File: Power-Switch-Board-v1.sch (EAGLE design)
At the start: 7 parts, among them U3 CPH3356-TL-W

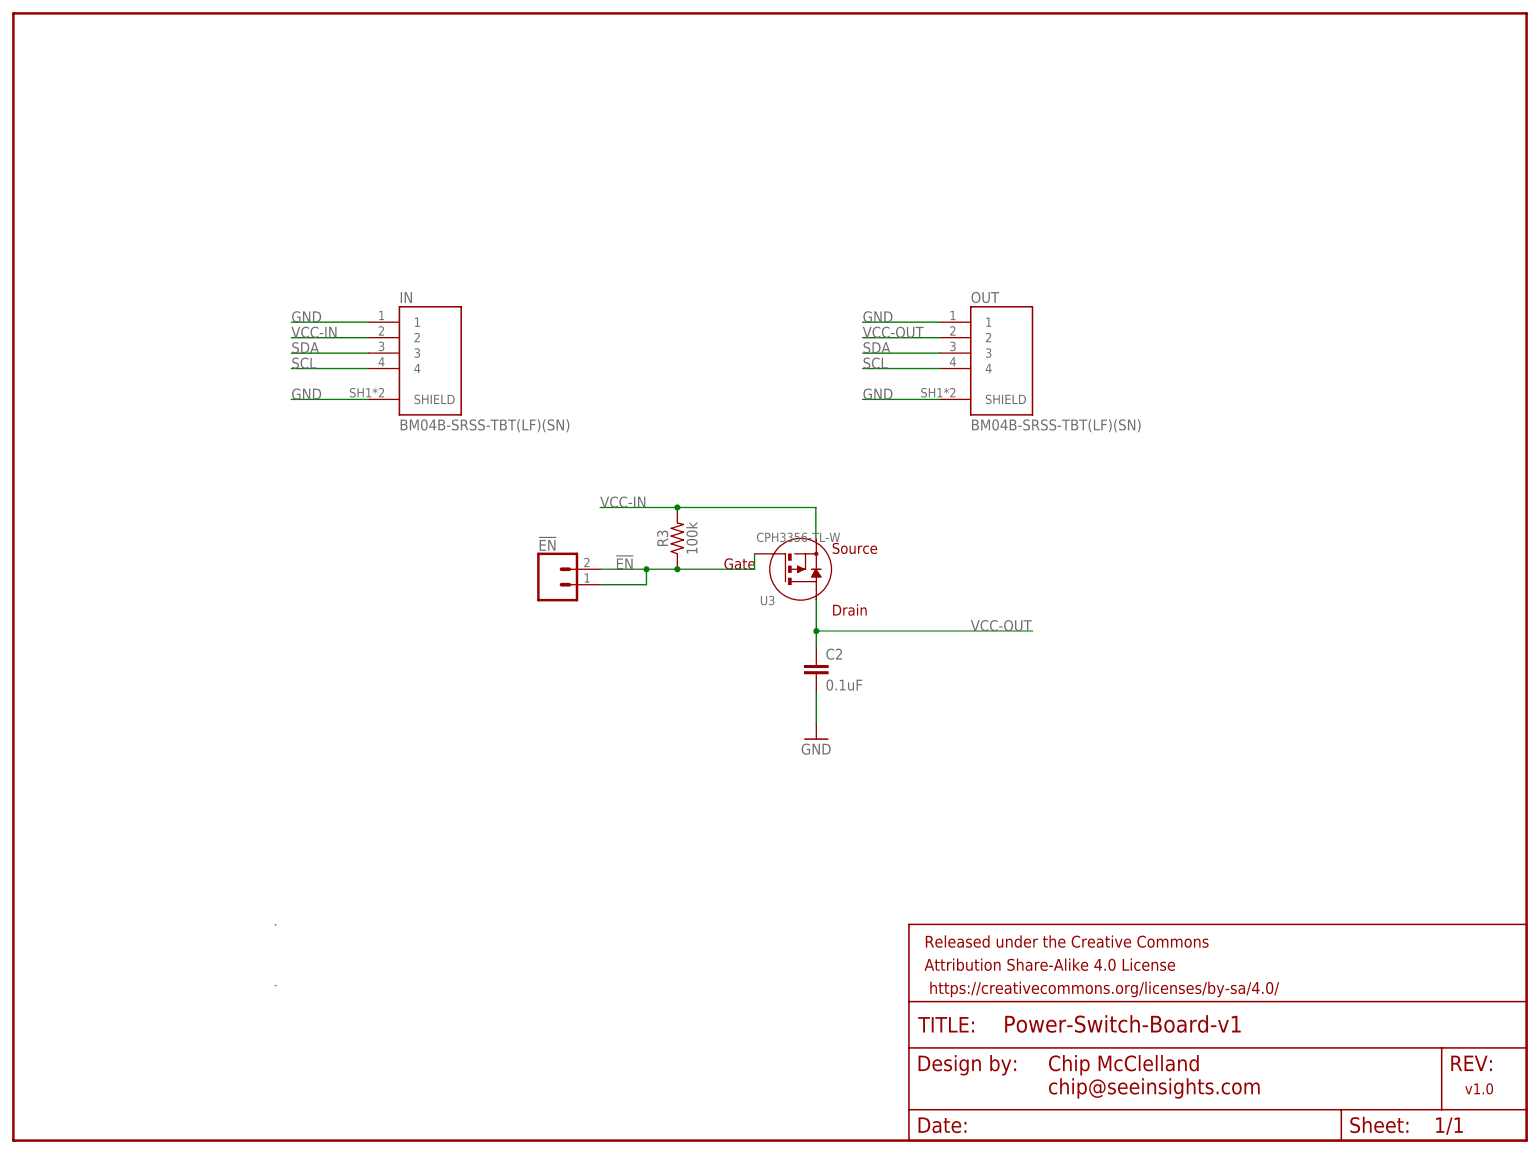
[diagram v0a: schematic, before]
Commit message: Updated for 0.1" headers
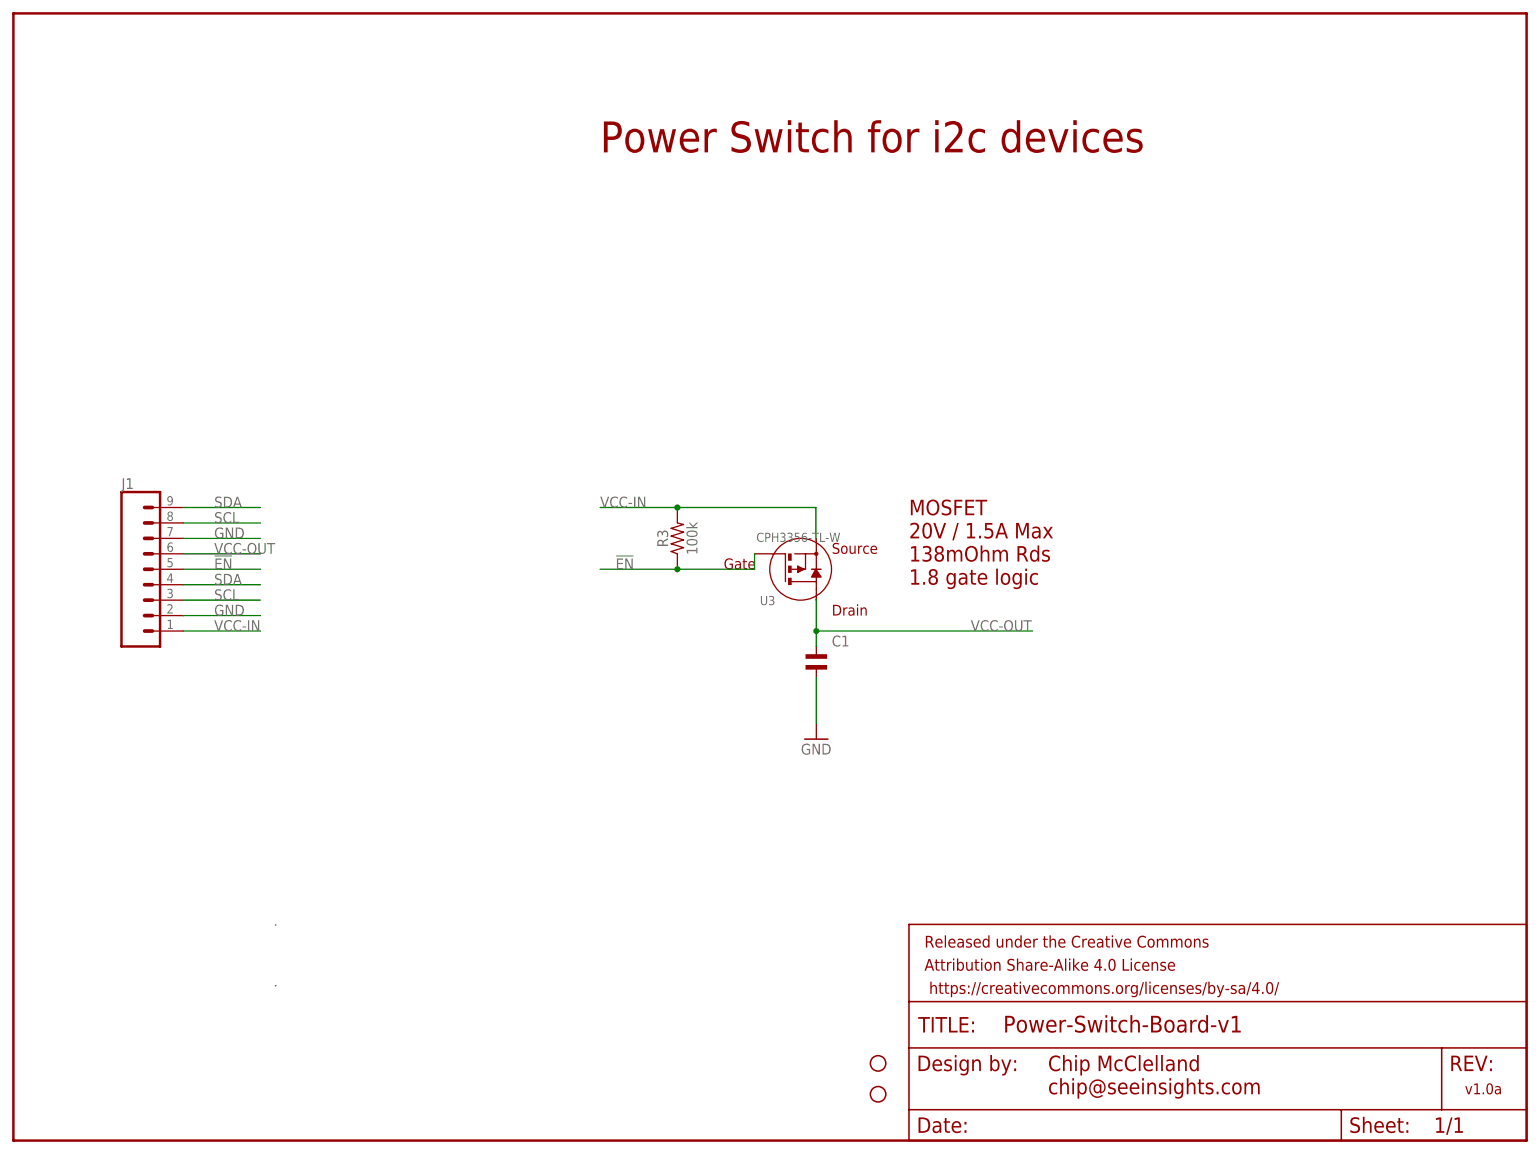
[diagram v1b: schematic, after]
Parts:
- removed !EN: (no value), SparkFun-Connectors:CONN_02
- removed C2: 0.1uF, Custom Components:CAP-MF-0.1UF-0805
- removed IN, OUT: BM04B-SRSS-TBT(LF)(SN), Custom Components:BM04B-SRSS-TBT(LF)(SN)
- added C1: (no value), Custom Components:CAP-MF-0.1UF-
- added H1, H2: STAND-OFF-M2.5, Custom Components:STAND-OFF-M2.5
- added J1: (no value), SparkFun-Connectors:CONN_09
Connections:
- net !EN: now also J1.5; no longer !EN.1, !EN.2
- net GND: now also C1.P$2, J1.2, J1.7; no longer C2.2, IN.1, IN.SHIELD, OUT.1, OUT.SHIELD
- net SCL: now also J1.3, J1.8; no longer IN.4, OUT.4
- net SDA: now also J1.4, J1.9; no longer IN.3, OUT.3
- net VCC-IN: now also J1.1; no longer IN.2
- net VCC-OUT: now also C1.P$1, J1.6; no longer C2.1, OUT.2
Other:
- note added: "MOSFET 20V / 1.5A Max 138mOhm Rds 1.8 gate logic"
- note added: "Power Switch for i2c devices"
- note added: "v1.0a"
- note removed: "v1.0"
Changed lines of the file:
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@@
 <part name="FRAME1" library="SparkFun-Aesthetics" library_urn="urn:adsk.eagle:library:507" deviceset="FRAME-LETTER" device="" package3d_urn="urn:adsk.eagle:package:37121/1"/>
 <part name="GND4" library="SparkFun-PowerSymbols" library_urn="urn:adsk.eagle:library:530" deviceset="GND" device=""/>
-<part name="C2" library="Custom Components" deviceset="CAP-MF-0.1UF-" device="0805" value="0.1uF"/>
 <part name="U3" library="Custom Components" deviceset="CPH3356-TL-W" device=""/>
 <part name="R3" library="Custom Components" deviceset="RESISTOR-MF-100K-" device="0805" package3d_urn="urn:adsk.eagle:package:39651/1" value="100k"/>
-<part name="IN" library="Custom Components" deviceset="BM04B-SRSS-TBT(LF)(SN)" device=""/>
-<part name="OUT" library="Custom Components" deviceset="BM04B-SRSS-TBT(LF)(SN)" device=""/>
-<part name="!EN" library="SparkFun-Connectors" library_urn="urn:adsk.eagle:library:513" deviceset="CONN_02" device="" package3d_urn="urn:adsk.eagle:package:38039/1"/>
+<part name="J1" library="SparkFun-Connectors" library_urn="urn:adsk.eagle:library:513" deviceset="CONN_09" device="" package3d_urn="urn:adsk.eagle:package:38153/1"/>
+<part name="H1" library="Custom Components" deviceset="STAND-OFF-M2.5" device="" package3d_urn="urn:adsk.eagle:package:38630/1"/>
+<part name="H2" library="Custom Components" deviceset="STAND-OFF-M2.5" device="" package3d_urn="urn:adsk.eagle:package:38630/1"/>
+<part name="C1" library="Custom Components" deviceset="CAP-MF-0.1UF-" device=""/>
 </parts>
 <sheets>
 <sheet>
 <plain>
-<text x="238.76" y="7.62" size="1.778" layer="94">v1.0</text>
+<text x="238.76" y="7.62" size="1.778" layer="94">v1.0a</text>
 <text x="170.18" y="7.62" size="2.54" layer="94">Chip McClelland
 chip@seeinsights.com</text>
+<text x="96.52" y="162.56" size="5.08" layer="94">Power Switch for i2c devices</text>
+<text x="147.32" y="91.44" size="2.54" layer="94">MOSFET
+20V / 1.5A Max
+138mOhm Rds
+1.8 gate logic</text>
 </plain>
 <instances>
@@
 <attribute name="VALUE" x="129.54" y="63.5" size="1.778" layer="96"/>
 </instance>
-<instance part="C2" gate="G$1" x="132.08" y="76.2" smashed="yes">
-<attribute name="MPN" x="132.08" y="76.2" size="1.778" layer="96" display="off"/>
-<attribute name="NAME" x="133.604" y="79.121" size="1.778" layer="95"/>
-<attribute name="VALUE" x="133.604" y="74.041" size="1.778" layer="96"/>
-</instance>
 <instance part="U3" gate="A" x="129.54" y="93.98" smashed="yes">
 <attribute name="VALUE" x="122.2" y="99.98" size="1.5" layer="96" ratio="0" rot="MR180"/>
@@
 <attribute name="MPN" x="109.22" y="99.06" size="1.778" layer="96" rot="R90" display="off"/>
 </instance>
-<instance part="IN" gate="G$1" x="68.58" y="127" smashed="yes">
-<attribute name="NAME" x="63.49978125" y="137.7955" size="1.77808125" layer="95"/>
-<attribute name="VALUE" x="63.495490625" y="116.831" size="1.77958125" layer="96"/>
+<instance part="J1" gate="G$1" x="17.78" y="93.98" smashed="yes">
+<attribute name="VALUE" x="17.78" y="78.994" size="1.778" layer="96" font="vector"/>
+<attribute name="NAME" x="17.78" y="107.188" size="1.778" layer="95" font="vector"/>
 </instance>
-<instance part="OUT" gate="G$1" x="162.56" y="127" smashed="yes">
-<attribute name="NAME" x="157.47978125" y="137.7955" size="1.77808125" layer="95"/>
-<attribute name="VALUE" x="157.475490625" y="116.831" size="1.77958125" layer="96"/>
-</instance>
-<instance part="!EN" gate="G$1" x="88.9" y="91.44" smashed="yes">
-<attribute name="VALUE" x="86.36" y="86.614" size="1.778" layer="96" font="vector"/>
-<attribute name="NAME" x="86.36" y="97.028" size="1.778" layer="95" font="vector"/>
+<instance part="H1" gate="G$1" x="142.24" y="12.7" smashed="yes"/>
+<instance part="H2" gate="G$1" x="142.24" y="7.62" smashed="yes"/>
+<instance part="C1" gate="G$1" x="132.08" y="78.74" smashed="yes">
+<attribute name="NAME" x="134.62" y="81.28" size="1.778" layer="95"/>
+<attribute name="VALUE" x="134.62" y="76.2" size="1.778" layer="96"/>
 </instance>
 </instances>
@@
 <net name="GND" class="0">
 <segment>
-<pinref part="GND4" gate="1" pin="GND"/>
-<wire x1="132.08" y1="73.66" x2="132.08" y2="68.58" width="0.1524" layer="91"/>
-<pinref part="C2" gate="G$1" pin="2"/>
+<wire x1="40.64" y1="86.36" x2="27.94" y2="86.36" width="0.1524" layer="91"/>
+<pinref part="J1" gate="G$1" pin="2"/>
+<label x="33.02" y="86.36" size="1.778" layer="95"/>
 </segment>
 <segment>
-<pinref part="IN" gate="G$1" pin="1"/>
-<wire x1="58.42" y1="134.62" x2="45.72" y2="134.62" width="0.1524" layer="91"/>
-<label x="45.72" y="134.62" size="1.778" layer="95"/>
+<wire x1="40.64" y1="99.06" x2="27.94" y2="99.06" width="0.1524" layer="91"/>
+<pinref part="J1" gate="G$1" pin="7"/>
+<label x="33.02" y="99.06" size="1.778" layer="95"/>
 </segment>
 <segment>
-<wire x1="152.4" y1="134.62" x2="139.7" y2="134.62" width="0.1524" layer="91"/>
-<pinref part="OUT" gate="G$1" pin="1"/>
-<label x="139.7" y="134.62" size="1.778" layer="95"/>
-</segment>
-<segment>
-<wire x1="58.42" y1="121.92" x2="45.72" y2="121.92" width="0.1524" layer="91"/>
-<pinref part="IN" gate="G$1" pin="SHIELD"/>
-<label x="45.72" y="121.92" size="1.778" layer="95"/>
-</segment>
-<segment>
-<wire x1="152.4" y1="121.92" x2="139.7" y2="121.92" width="0.1524" layer="91"/>
-<pinref part="OUT" gate="G$1" pin="SHIELD"/>
-<label x="139.7" y="121.92" size="1.778" layer="95"/>
+<pinref part="C1" gate="G$1" pin="P$2"/>
+<pinref part="GND4" gate="1" pin="GND"/>
+<wire x1="132.08" y1="76.2" x2="132.08" y2="68.58" width="0.1524" layer="91"/>
 </segment>
 </net>
 <net name="!EN" class="0">
 <segment>
-<wire x1="96.52" y1="93.98" x2="104.14" y2="93.98" width="0.1524" layer="91"/>
+<wire x1="96.52" y1="93.98" x2="109.22" y2="93.98" width="0.1524" layer="91"/>
 <pinref part="R3" gate="G$1" pin="1"/>
 <pinref part="U3" gate="A" pin="GATE"/>
-<wire x1="104.14" y1="93.98" x2="109.22" y2="93.98" width="0.1524" layer="91"/>
 <wire x1="109.22" y1="93.98" x2="121.92" y2="93.98" width="0.1524" layer="91"/>
 <wire x1="121.92" y1="93.98" x2="121.92" y2="96.52" width="0.1524" layer="91"/>
 <junction x="109.22" y="93.98"/>
 <label x="99.06" y="93.98" size="1.778" layer="95"/>
-<pinref part="!EN" gate="G$1" pin="2"/>
-<pinref part="!EN" gate="G$1" pin="1"/>
-<wire x1="96.52" y1="91.44" x2="104.14" y2="91.44" width="0.1524" layer="91"/>
-<wire x1="104.14" y1="91.44" x2="104.14" y2="93.98" width="0.1524" layer="91"/>
-<junction x="104.14" y="93.98"/>
+</segment>
+<segment>
+<wire x1="27.94" y1="93.98" x2="40.64" y2="93.98" width="0.1524" layer="91"/>
+<pinref part="J1" gate="G$1" pin="5"/>
+<label x="33.02" y="93.98" size="1.778" layer="95"/>
 </segment>
 </net>
@@
 </segment>
 <segment>
-<pinref part="IN" gate="G$1" pin="2"/>
-<wire x1="58.42" y1="132.08" x2="45.72" y2="132.08" width="0.1524" layer="91"/>
-<label x="45.72" y="132.08" size="1.778" layer="95"/>
+<wire x1="40.64" y1="83.82" x2="27.94" y2="83.82" width="0.1524" layer="91"/>
+<pinref part="J1" gate="G$1" pin="1"/>
+<label x="33.02" y="83.82" size="1.778" layer="95"/>
 </segment>
 </net>
@@
 <segment>
 <label x="157.48" y="83.82" size="1.778" layer="95"/>
-<pinref part="C2" gate="G$1" pin="1"/>
 <wire x1="132.08" y1="83.82" x2="132.08" y2="81.28" width="0.1524" layer="91"/>
 <wire x1="132.08" y1="83.82" x2="167.64" y2="83.82" width="0.1524" layer="91"/>
@@
 <wire x1="132.08" y1="88.98" x2="132.08" y2="83.82" width="0.1524" layer="91"/>
 <junction x="132.08" y="83.82"/>
+<pinref part="C1" gate="G$1" pin="P$1"/>
 </segment>
 <segment>
-<wire x1="152.4" y1="132.08" x2="139.7" y2="132.08" width="0.1524" layer="91"/>
-<pinref part="OUT" gate="G$1" pin="2"/>
-<label x="139.7" y="132.08" size="1.778" layer="95"/>
+<wire x1="40.64" y1="96.52" x2="27.94" y2="96.52" width="0.1524" layer="91"/>
+<pinref part="J1" gate="G$1" pin="6"/>
+<label x="33.02" y="96.52" size="1.778" layer="95"/>
 </segment>
 </net>
 <net name="SCL" class="0">
 <segment>
-<pinref part="IN" gate="G$1" pin="4"/>
-<wire x1="58.42" y1="127" x2="45.72" y2="127" width="0.1524" layer="91"/>
-<label x="45.72" y="127" size="1.778" layer="95"/>
+<wire x1="40.64" y1="88.9" x2="27.94" y2="88.9" width="0.1524" layer="91"/>
+<pinref part="J1" gate="G$1" pin="3"/>
+<label x="33.02" y="88.9" size="1.778" layer="95"/>
 </segment>
 <segment>
-<wire x1="152.4" y1="127" x2="139.7" y2="127" width="0.1524" layer="91"/>
-<pinref part="OUT" gate="G$1" pin="4"/>
-<label x="139.7" y="127" size="1.778" layer="95"/>
+<wire x1="40.64" y1="101.6" x2="27.94" y2="101.6" width="0.1524" layer="91"/>
+<pinref part="J1" gate="G$1" pin="8"/>
+<label x="33.02" y="101.6" size="1.778" layer="95"/>
 </segment>
 </net>
 <net name="SDA" class="0">
 <segment>
-<pinref part="IN" gate="G$1" pin="3"/>
-<wire x1="58.42" y1="129.54" x2="45.72" y2="129.54" width="0.1524" layer="91"/>
-<label x="45.72" y="129.54" size="1.778" layer="95"/>
+<wire x1="40.64" y1="91.44" x2="27.94" y2="91.44" width="0.1524" layer="91"/>
+<pinref part="J1" gate="G$1" pin="4"/>
+<label x="33.02" y="91.44" size="1.778" layer="95"/>
 </segment>
 <segment>
-<wire x1="152.4" y1="129.54" x2="139.7" y2="129.54" width="0.1524" layer="91"/>
-<pinref part="OUT" gate="G$1" pin="3"/>
-<label x="139.7" y="129.54" size="1.778" layer="95"/>
+<wire x1="40.64" y1="104.14" x2="27.94" y2="104.14" width="0.1524" layer="91"/>
+<pinref part="J1" gate="G$1" pin="9"/>
+<label x="33.02" y="104.14" size="1.778" layer="95"/>
 </segment>
 </net>
